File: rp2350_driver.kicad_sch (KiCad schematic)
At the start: 194 parts, among them J19 Conn_01x03, J201 Estop Conn, J202 USB_C_Receptacle_USB2.0, J203 Conn_01x06, J204 SM03B-SRSS-TB, J206 SM03B-SRSS-TB, J21 Power Input, Q1 Q_PNP_BEC, Q2 Q_PNP_BEC, Q3 Q_PNP_BEC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

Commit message: Add 4th bridge, update connectors
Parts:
- added C220: 4.7uF 35V, Capacitor_SMD:C_0603_1608Metric, symbol Device:C
- added C233: DNP, Capacitor_SMD:C_0603_1608Metric, symbol Device:C
- added C234, C235: C, Capacitor_SMD:C_0805_2012Metric, symbol Device:C
- added C236: 10uF 35v, Capacitor_SMD:C_0603_1608Metric, symbol Device:C
- added CH201, CL201: MOSFETSO-8, parts:PowerPAK_SO-8_123, symbol Device:Q_NMOS_SGD
- added D203: FR107, Diode_SMD:D_SOD-123, symbol Device:D
- added D204, D205: CDBU0130R-HF, Diode_SMD:D_SOD-523, symbol Device:D
- added D206: SMAJ51A, Diode_SMD:D_SMA, symbol Diode:SMF54A
- added Q201: Q_PNP_BEC, Package_TO_SOT_SMD:SOT-23, symbol Device:Q_PNP_BEC
- added R227, R228: 10k, Resistor_SMD:R_0603_1608Metric, symbol MotorController:TAYLOR_RESISTOR
- added R229, R230, R232: 0R, Resistor_SMD:R_0603_1608Metric, symbol MotorController:TAYLOR_RESISTOR
- added R231: 100R, Resistor_SMD:R_0603_1608Metric, symbol MotorController:TAYLOR_RESISTOR
- added R233, R234, R235: 10.2R, Resistor_SMD:R_0603_1608Metric, symbol MotorController:TAYLOR_RESISTOR
- added R236, R237: R, Resistor_SMD:R_0805_2012Metric, symbol Device:R
- added TP207, TP208: TestPoint, parts:TestPoint_Pad_D1.5mm_no_courtyard, symbol Connector:TestPoint
- added U201: EG3113, Package_SO:SOIC-8_3.9x4.9mm_P1.27mm, symbol MotorBuck:EG2131
- J19: footprint Connector_AMASS:AMASS_MR30PW-M_1x03_P3.50mm_Horizontal -> Connector_Molex:Molex_Sabre_46007-1104_1x04_P7.49mm_Horizontal; symbol Connector_Generic:Conn_01x03 -> Connector_Generic:Conn_01x04; Digikey (none) -> 0431601104
- J203: footprint parts:Molex_KK-254_1x06_P2.54mm_Horizontal -> Connector_Molex:Molex_Micro-Fit_3.0_43045-1010_2x05-1MP_P3.00mm_Horizontal; symbol Connector_Generic:Conn_01x06 -> Connector_Generic:Conn_02x05_Top_Bottom; LCSC C2982045 -> C19189870
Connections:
- net +3V3: no longer J203.2 (Pin_2)
- net +5V: now also C220.2, D203.2 (A), U201.1 (VCC)
- net ENC1_CS: no longer J203.4 (Pin_4)
- net ENC1_RX: no longer J203.3 (Pin_3)
- net ENC1_SCK: no longer J203.5 (Pin_5)
- net GND: now also C220.1, C233.1, C235.2, CL201.1 (S), D206.2 (A2), Q201.3 (C), R227.1, R228.1, U201.4 (COM); no longer J203.6 (Pin_6)
- net TH_MOTOR1: no longer J203.1 (Pin_1)
- net VMOT: now also CH201.3 (D), R236.1
- new net: Q201.2 (E), R235.1
- new net: R230.1, R234.1, U201.7 (HO)
- new net: D204.1 (K), R230.2
- new net: D203.1 (K), R229.1
- new net: R231.1, R232.1, R233.1, U201.5 (LO)
- new net: C235.1, R237.2
- new net: C236.2, R229.2, U201.8 (VB)
- new net: Q201.1 (B), R231.2
- new net: D205.1 (K), R232.2
- new net: C234.1, R236.2
- new net 2DGH: CH201.2 (G), D204.2 (A), R234.2, TP207.1
- new net 2DGL: C233.2, CL201.2 (G), D205.2 (A), R233.2, R235.2, TP208.1
- new net D: C234.2, C236.1, CH201.1 (S), CL201.3 (D), D206.1 (A1), J19.4 (Pin_4), R237.1, U201.6 (VS)
- new net D_PWM_H: R227.2, U201.2 (HIN)
- new net D_PWM_L\: R228.2, U201.3 (~{LIN})

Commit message: Refine design rules, make cpu fit rules, add gitignore
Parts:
- added D207: 3.3v Zener, Diode_SMD:D_SOD-123, symbol Device:D_Zener
- added H1: MountingHole, parts:MountingHole_3.9mm_Plastite_#6, symbol Mechanical:MountingHole
- added J205: Power Output, Connector_AMASS:AMASS_XT30PW-F_1x02_P2.50mm_Horizontal, symbol Connector_Generic:Conn_01x02
- added J207: Conn_01x03, Connector_PinHeader_2.54mm:PinHeader_1x03_P2.54mm_Horizontal, symbol Connector_Generic:Conn_01x03
- added J208: Conn_01x03, Connector_PinSocket_2.54mm:PinSocket_1x03_P2.54mm_Horizontal, symbol Connector_Generic:Conn_01x03
- added R238, R239: 50k 0.1%, Resistor_SMD:R_0603_1608Metric, symbol MotorController:TAYLOR_RESISTOR
- added R240: 5.1k 0.1%, Resistor_SMD:R_0603_1608Metric, symbol MotorController:TAYLOR_RESISTOR
- U4: value ~ -> TX4137
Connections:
- net GND: now also D207.2 (A), J205.1 (Pin_1), R240.2
- net VMOT: now also J205.2 (Pin_2), R238.1
- net V_ENABLE: now reaches U4.4 (EN)
- net V_ENABLE: now also D207.1 (K), R239.2, R240.1
- new net: R238.2, R239.1
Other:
- note removed: "Double check enable"
- note removed: "FIGURE OUT ENABLE"
- moved on the sheet: C10, C12, C201, C202, D3, L1, R11, R12, U202, U4

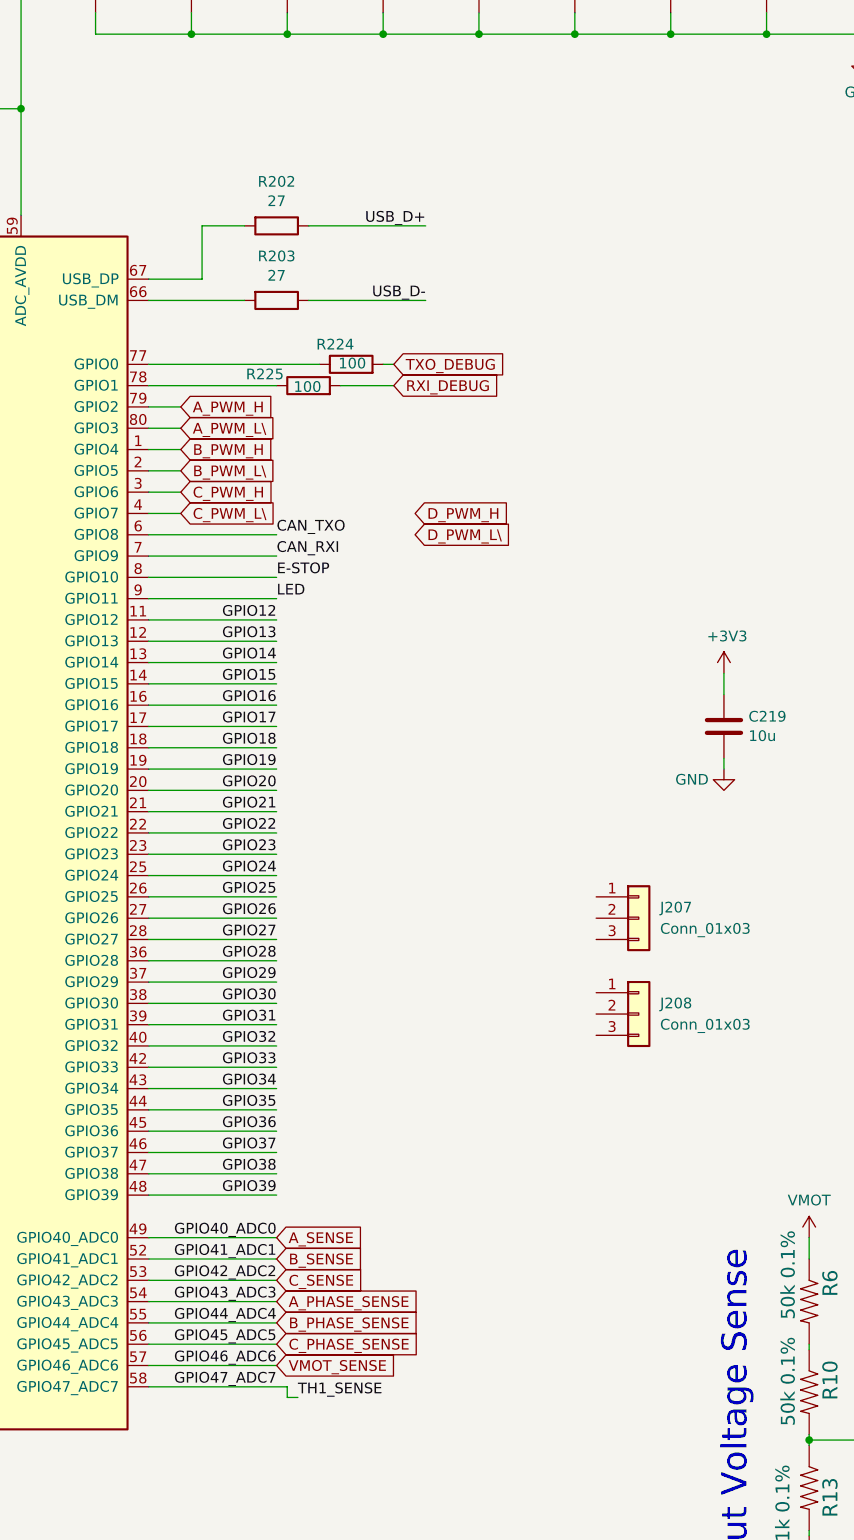
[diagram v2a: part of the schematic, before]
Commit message: adjust stackup, rotate CPU, update via and trace defaults
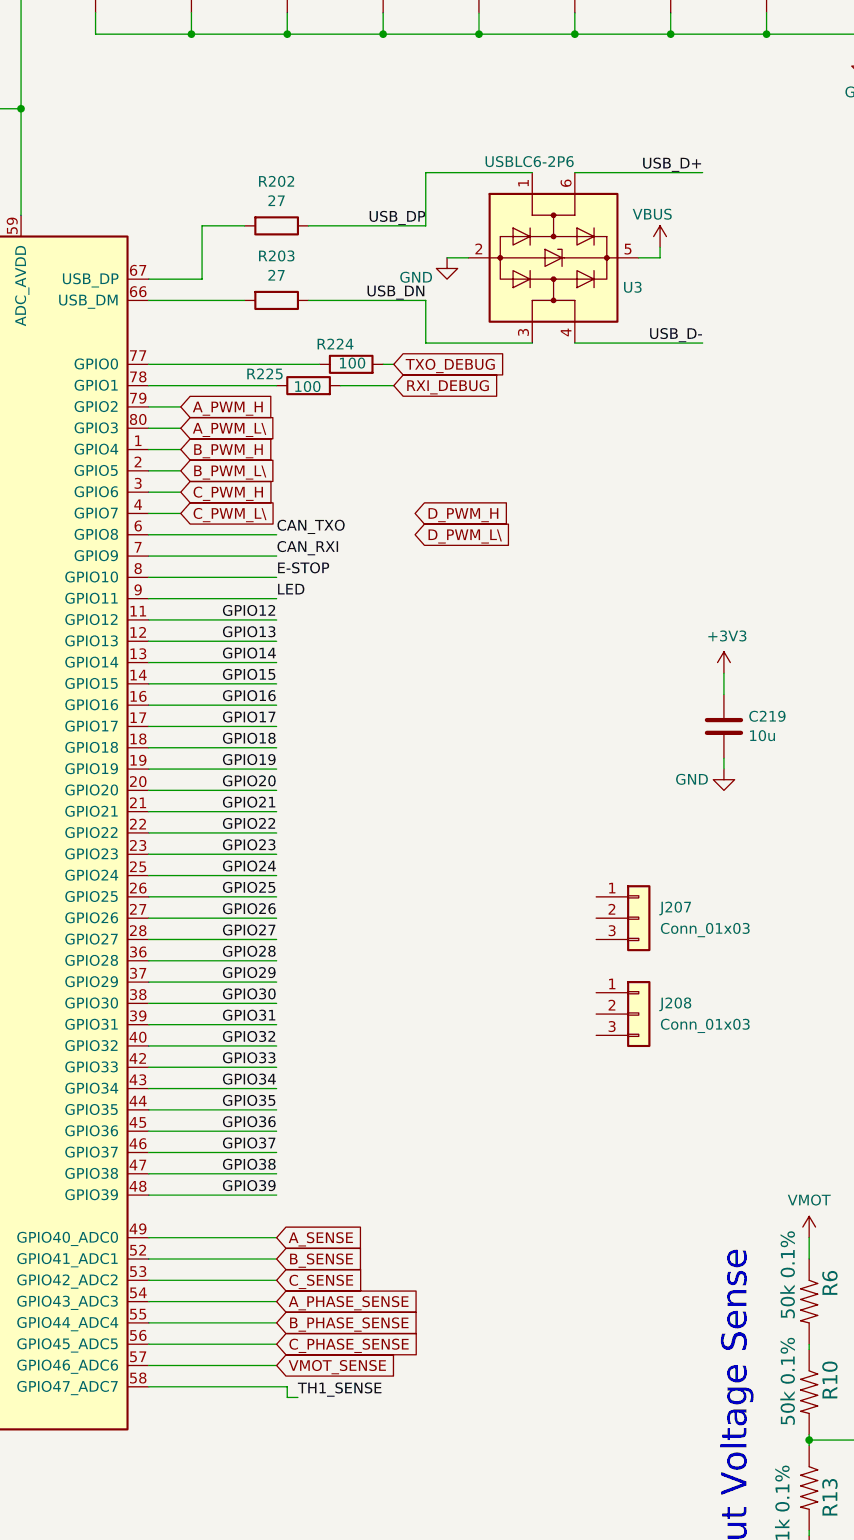
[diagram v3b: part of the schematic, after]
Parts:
- added U3: USBLC6-2P6, Package_TO_SOT_SMD:SOT-666, symbol Power_Protection:USBLC6-2P6
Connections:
- net GND: now also U3.2 (GND)
- net USB_D+: now also U3.6 (I/O1); no longer R202.1
- net USB_D-: now also U3.4 (I/O2); no longer R203.1
- net VBUS: now also U3.5 (VBUS)
- net GPIO47_ADC7 renamed TH1_SENSE
- new net USB_DN: R203.1, U3.3 (I/O2)
- new net USB_DP: R202.1, U3.1 (I/O1)

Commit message: refining layout, beginning to sort out differential encoders
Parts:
- removed J19: Conn_01x03, Connector_Molex:Molex_Sabre_46007-1104_1x04_P7.49mm_Horizontal, symbol Connector_Generic:Conn_01x04
- added C5: 100n, Capacitor_SMD:C_0603_1608Metric, symbol Device:C
- added C7: 4.7uF 35V, Capacitor_SMD:C_0603_1608Metric, symbol Device:C
- added C8: 100n, Capacitor_SMD:C_0402_1005Metric, symbol Device:C
- added D4: ESDCAN24-2BLY, Package_TO_SOT_SMD:SOT-23, symbol Power_Protection:NUP2105L
- added H2, H3, H4: MountingHole, parts:MountingHole_3.9mm_Plastite_#6, symbol Mechanical:MountingHole
- added J1, J3: Power Input, Connector_AMASS:AMASS_XT30PW-M_1x02_P2.50mm_Horizontal, symbol Connector_Generic:Conn_01x02
- added J2: CAN2 PLUG, parts:PINREX-744-81-04TW00 _1x04_P2.54mm_Vertical, symbol Connector_Generic:Conn_01x04
- added R14: 100R 0402, Resistor_SMD:R_0402_1005Metric, symbol Device:R_Small
- added U12: MAX3485, Package_SO:SOIC-8_3.9x4.9mm_P1.27mm, symbol Interface_UART:MAX3485
- added U6: CA-IS3052G, Package_SO:SOIC-8_7.5x5.85mm_P1.27mm, symbol motor_parts:CA-IS3052G
- J203: footprint Connector_Molex:Molex_Micro-Fit_3.0_43045-1010_2x05-1MP_P3.00mm_Horizontal -> parts:CONN12_5018761240_MOL; LCSC C19189870 -> C493440
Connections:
- net CAN_RXI is gone; now on net D_PWM_L\: U203.7 (GPIO9)
- net CAN_TXO is gone; now on net D_PWM_H: U203.6 (GPIO8)
- net GPIO12 is gone; now on net TXO_INTERBOARD_1: U203.11 (GPIO12)
- net GPIO13 is gone; now on net RXI_INTERBOARD_1: U203.12 (GPIO13)
- net GPIO24 is gone; now on net TXO_INTERBOARD_2: U203.25 (GPIO24)
- net GPIO25 is gone; now on net RXI_INTERBOARD_2: U203.26 (GPIO25)
- net +3V3: now also C8.1, U6.1 (VCC1)
- net A_N: now also J1.1 (Pin_1)
- net B_N: now also J3.2 (Pin_2)
- net C_N: now also J3.1 (Pin_1)
- net D: now also J1.2 (Pin_2)
- net GND: now also J207.3 (Pin_3), J208.3 (Pin_3), C8.2, U6.4 (GND1)
- net TXO_INTERBOARD_1: now reaches J207.1 (Pin_1)
- net RXI_INTERBOARD_1: now reaches J207.2 (Pin_2)
- net RXI_INTERBOARD_2: now reaches J208.1 (Pin_1)
- net TXO_INTERBOARD_2: now reaches J208.2 (Pin_2)
- net GPIO20 renamed CAN_CPU_TXO
- net CAN_CPU_TXO: now also U6.2 (TXD)
- net GPIO21 renamed CAN_CPU_RXI
- net CAN_CPU_RXI: now also U6.3 (RXD)
- new net +5V_ISO: J2.1 (Pin_1)
- new net +5V_ISO_FILT: C5.2, C7.2, U6.8 (VCC2)
- new net CAN0_N: D4.2 (K), J2.3 (Pin_3), U6.6 (CANL)
- new net CAN0_P: D4.1 (K), J2.2 (Pin_2), U6.7 (CANH)
- new net ENC_A_N: R14.1, U12.7 (B)
- new net ENC_A_P: R14.2, U12.6 (A)
- new net GND_ISO: C5.1, C7.1, D4.3 (A), J2.4 (Pin_4), U6.5 (GND2)
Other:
- note added: "(ENC_CS)"
- note added: "(ENC_RX)"
- note added: "(ENC_SCK)"
- note added: "ENCODER NEEDS LEVEL SHIFTERS"
- note added: "Preferred connections: Differential I2C (Will choose single ended for now) Hall Sensors (single ended) Differential SPI Differential Quadrature with Index No planned support for analog (could add SPI converter)"
- moved on the sheet: C219, C223, C224, C225, C226, C227, C228, C229, C230, C231, C232, C4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

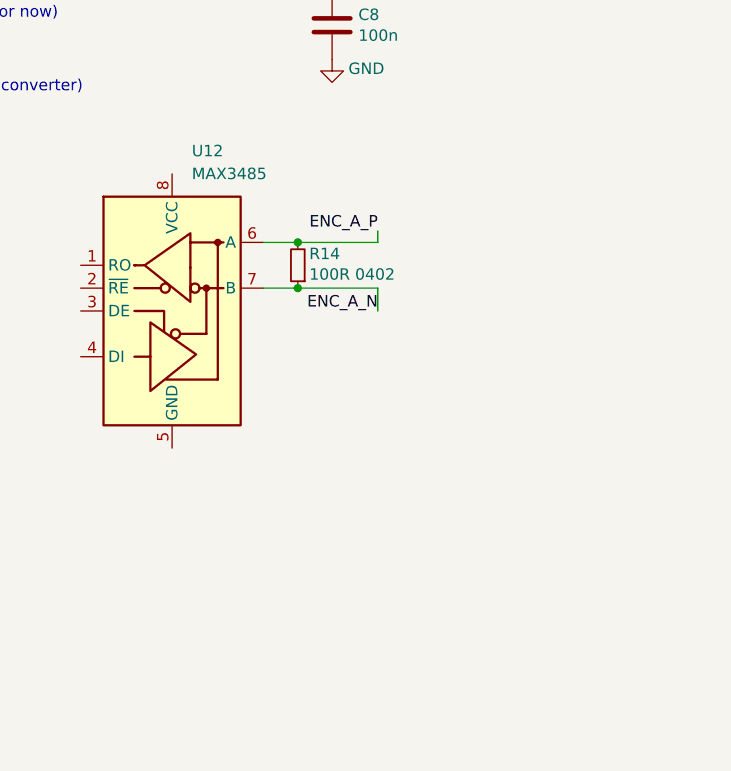
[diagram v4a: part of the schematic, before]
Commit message: progress on encoder connector and differential IC selection
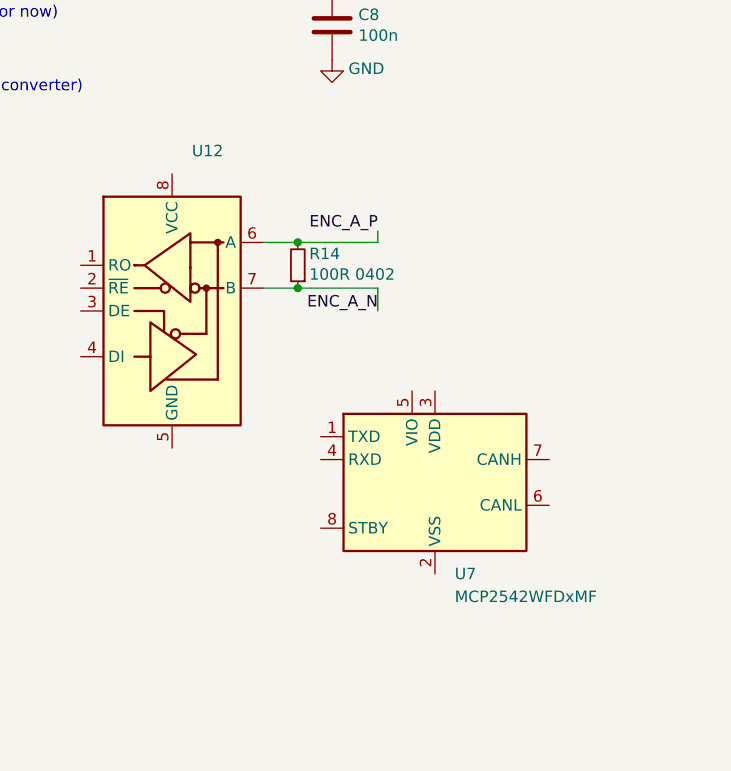
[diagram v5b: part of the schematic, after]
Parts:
- added U7: MCP2542WFDxMF, Package_DFN_QFN:DFN-8-1EP_3x3mm_P0.65mm_EP1.55x2.4mm, symbol Interface_CAN_LIN:MCP2542WFDxMF
- J203: Note (none) -> Possible board to board mating connector: VERIFY C3012189
- U12: value MAX3485 -> ~; footprint Package_SO:SOIC-8_3.9x4.9mm_P1.27mm -> parts:DFN-8_L3.0-W3.0-P0.65-BL-EP; LCSC (none) -> C601076; Web (none) -> https://www.lcsc.com/product-detail/RS-485-RS-422-ICs_SIT-S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
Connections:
- new net: U7.2 (VSS), U7.9 (VSS)
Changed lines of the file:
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@@
 			)
 		)
-		(property "Value" "MAX3485"
+		(property "Value" "~"
 			(at 713.3941 90.17 0)
 			(effects
@@
 			)
 		)
-		(property "Footprint" "Package_SO:SOIC-8_3.9x4.9mm_P1.27mm"
+		(property "Footprint" "parts:DFN-8_L3.0-W3.0-P0.65-BL-EP"
 			(at 711.2 128.27 0)
 			(effects
@@
 			)
 		)
-		(property "Datasheet" "https://datasheets.maximintegrated.com/en/ds/MAX3483-MAX3491.pdf"
+		(property "Datasheet" "https://www.lcsc.com/datasheet/lcsc_datasheet_2410091412_SIT-SIT3088ETK_C601076.pdf"
 			(at 711.2 104.14 0)
 			(effects
@@
 			)
 		)
-		(property "Description" "True RS-485/RS-422, 10Mbps, Slew-Rate Limited, with low-power shutdown, with receiver/driver enable, 32 receiver drive capacitity, DIP-8 and SOIC-8"
+		(property "Description" "Transceiver 14Mbps DFN-8-EP(3x3) RS-485 / RS-422 ICs ROHS"
+			(at 711.2 105.41 0)
+			(effects
+				(font
+					(size 1.27 1.27)
+				)
+				(hide yes)
+			)
+		)
+		(property "LCSC" "C601076"
+			(at 711.2 105.41 0)
+			(effects
+				(font
+					(size 1.27 1.27)
+				)
+				(hide yes)
+			)
+		)
+		(property "Web" "https://www.lcsc.com/product-detail/RS-485-RS-422-ICs_SIT-SIT3088ETK_C601076.html"
 			(at 711.2 105.41 0)
 			(effects
@@
 			)
 		)
+		(property "Note" "Possible board to board mating connector: VERIFY C3012189"
+			(at 648.97 102.87 0)
+			(effects
+				(font
+					(size 1.27 1.27)
+				)
+				(hide yes)
+			)
+		)
 		(pin "6"
 		)
@@
 					(unit 1)
 				)
+			)
+		)
+	)
+	(symbol
+		(lib_id "Interface_CAN_LIN:MCP2542WFDxMF")
+		(at 740.41 124.46 0)
+		(unit 1)
+		(exclude_from_sim no)
+		(in_bom yes)
+		(on_board yes)
+		(dnp no)
+		(fields_autoplaced yes)
+		(property "Reference" "U7"
+			(at 742.6041 134.62 0)
+			(effects
+				(font
+					(size 1.27 1.27)
+				)
+				(justify left)
+			)
+		)
+		(property "Value" "MCP2542WFDxMF"
+			(at 742.6041 137.16 0)
+			(effects
+				(font
+					(size 1.27 1.27)
+				)
+				(justify left)
+			)
+		)
+		(property "Footprint" "Package_DFN_QFN:DFN-8-1EP_3x3mm_P0.65mm_EP1.55x2.4mm"
+			(at 740.41 137.16 0)
+			(effects
+				(font
+					(size 1.27 1.27)
+					(italic yes)
+				)
+				(hide yes)
+			)
+		)
+		(property "Datasheet" "http://ww1.microchip.com/downloads/en/DeviceDoc/MCP2542FD-4FD-MCP2542WFD-4WFD-Data-Sheet20005514B.pdf"
+			(at 740.41 124.46 0)
+			(effects
+				(font
+					(size 1.27 1.27)
+				)
+				(hide yes)
+			)
+		)
+		(property "Description" "CAN-FD Transceiver, Wake-Up on CAN Pattern, 8Mbps, 5V supply, STBY pin, 3x3 DFN-8"
+			(at 740.41 124.46 0)
+			(effects
+				(font
+					(size 1.27 1.27)
+				)
+				(hide yes)
+			)
+		)
+		(pin "5"
+		)
+		(pin "2"
+		)
+		(pin "3"
+		)
+		(pin "9"
+		)
+		(pin "8"
+		)
+		(pin "4"
+		)
+		(pin "7"
+		)
+		(pin "6"
+		)
+		(pin "1"
+		)
+		(instances
+			(project ""
+				(path "/889c04f7-ab14-429c-99d2-ed773c17e58f"
+					(reference "U7")
+					(unit 1)
+				)
